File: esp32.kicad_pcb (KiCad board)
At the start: 2 copper layers, 44 x 80 mm, 102 parts, among them J1 USB_C, J14 PWR_CONN, J15 SPI_0, J16 SPI_1, J3 A0, J4 A1, J5 A2, J6 D0, J7 D1, J8 USB_VOUT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

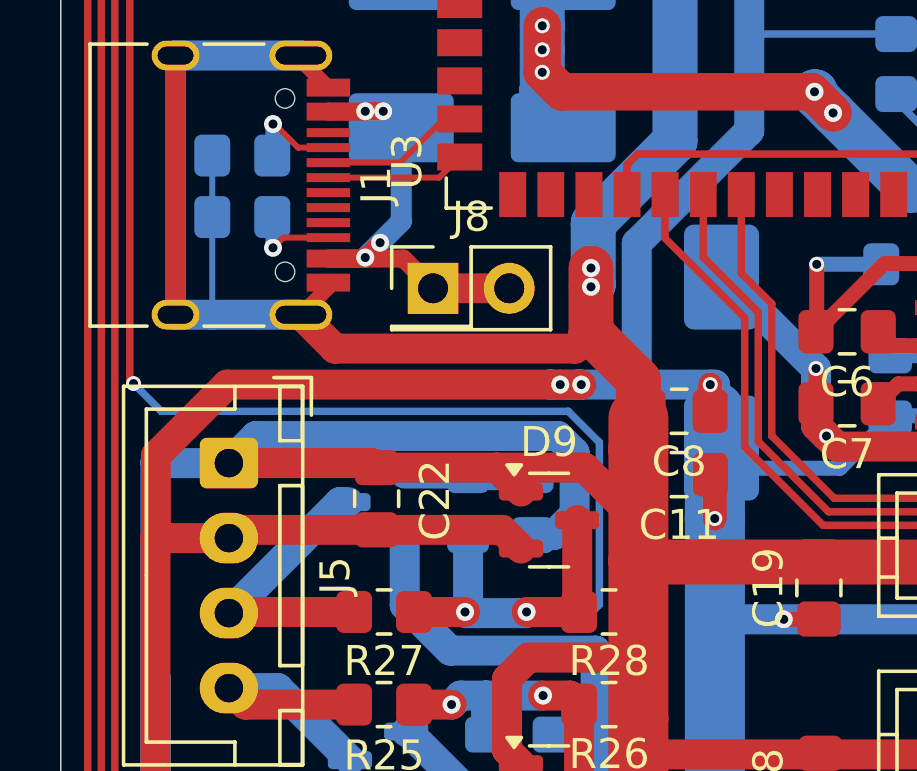
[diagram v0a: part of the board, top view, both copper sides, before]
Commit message: change footprint of Vusb
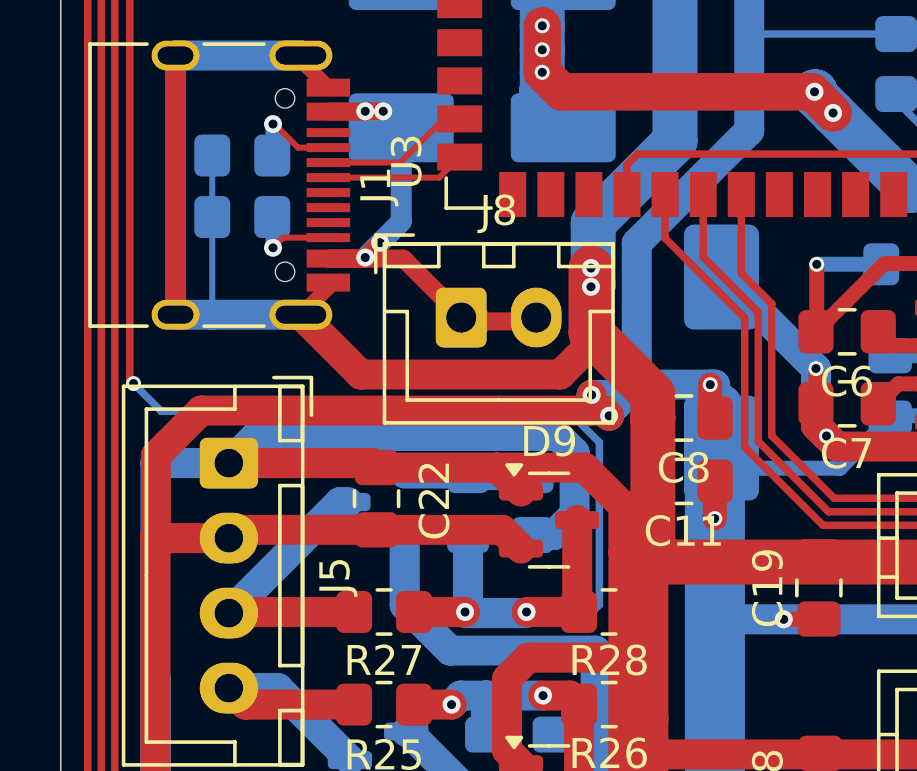
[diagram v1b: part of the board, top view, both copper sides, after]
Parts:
- J8: footprint Connector_PinHeader_2.54mm:PinHeader_2x01_P2.54mm_Vertical -> Connector_JST:JST_XH_B2B-XH-A_1x02_P2.50mm_Vertical
- moved J8 1.35 mm to (84.2, 96.6)
- moved C8 0.28 mm to (91.7, 100.0)
- moved C11 0.28 mm to (91.7, 102.1)
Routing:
- net GND: track 714.9 -> 717.8 mm
- net +3V3: track 446.4 -> 448.5 mm
- net V_USB: track 17.9 -> 19.6 mm

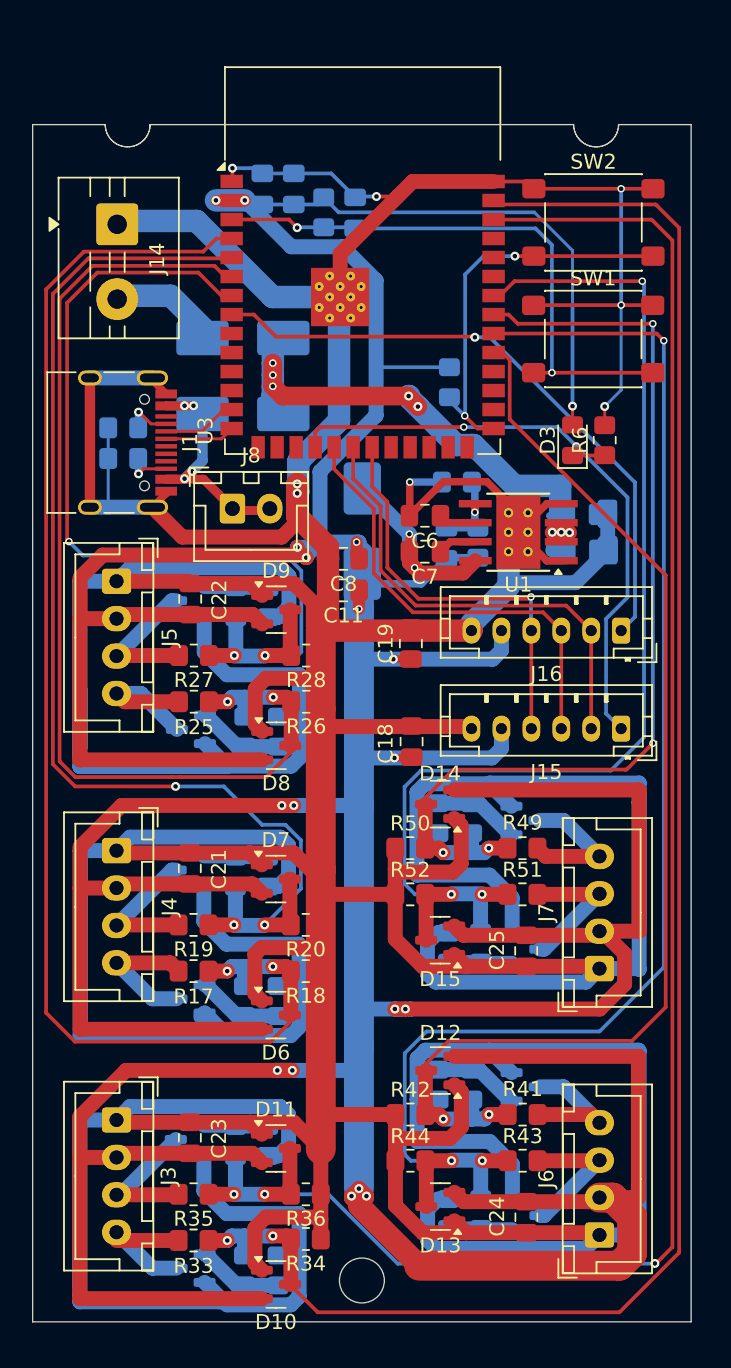
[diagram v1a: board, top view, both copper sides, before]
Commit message: move inductor
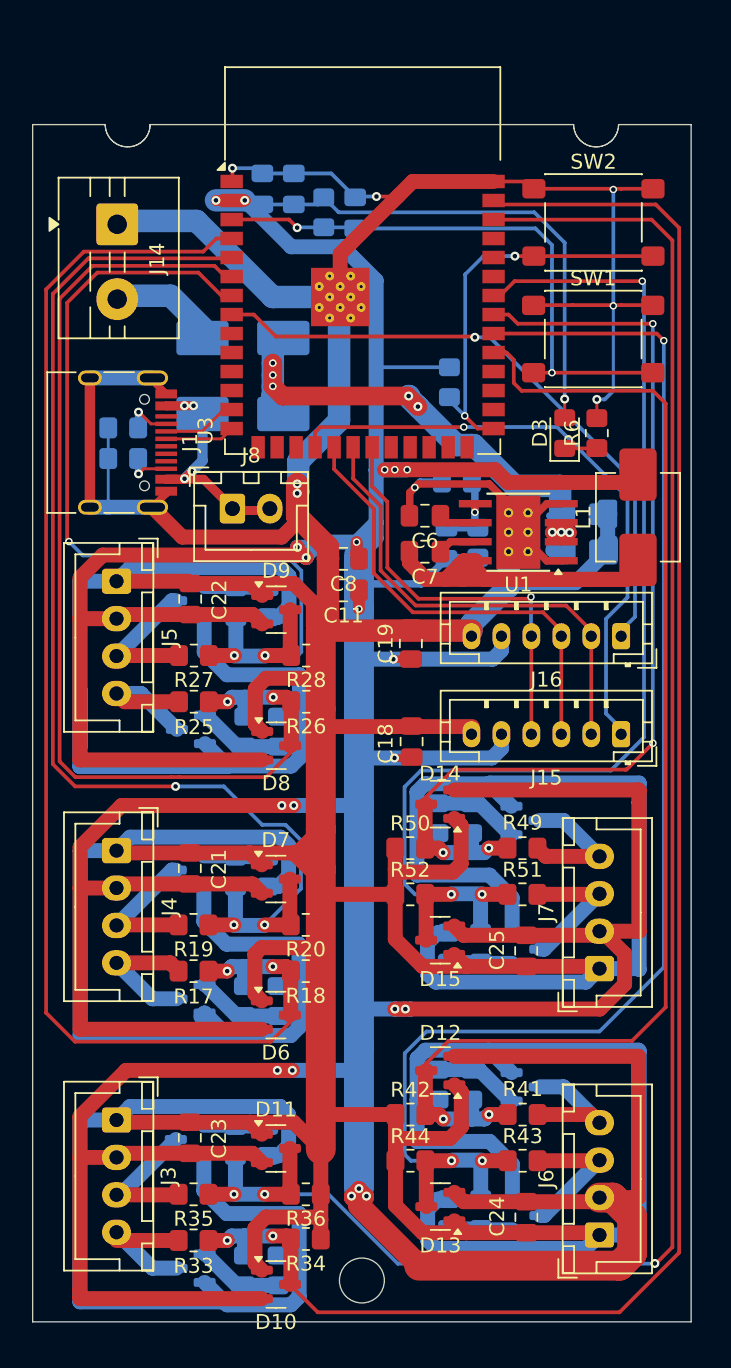
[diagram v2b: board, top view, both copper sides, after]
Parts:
- L1: moved to F.Cu
- moved L1 18.4 mm to (111.3, 97.2), turned to 90 degrees
- moved D3 0.71 mm to (106.4, 91.6)
- moved R6 0.71 mm to (108.6, 91.6)
- moved J15 0.38 mm to (110.2, 111.7)
- moved J16 0.38 mm to (110.2, 105.2)
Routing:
- net +3V3: track 448.5 -> 470.4 mm, vias 18 -> 21
- net Net-(U1-SW): track 13.7 -> 32.9 mm, vias 2 -> 0
- net /D0: track 76.3 -> 82.2 mm
- net GND: track 717.8 -> 718.5 mm

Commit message: fix power supply module layout
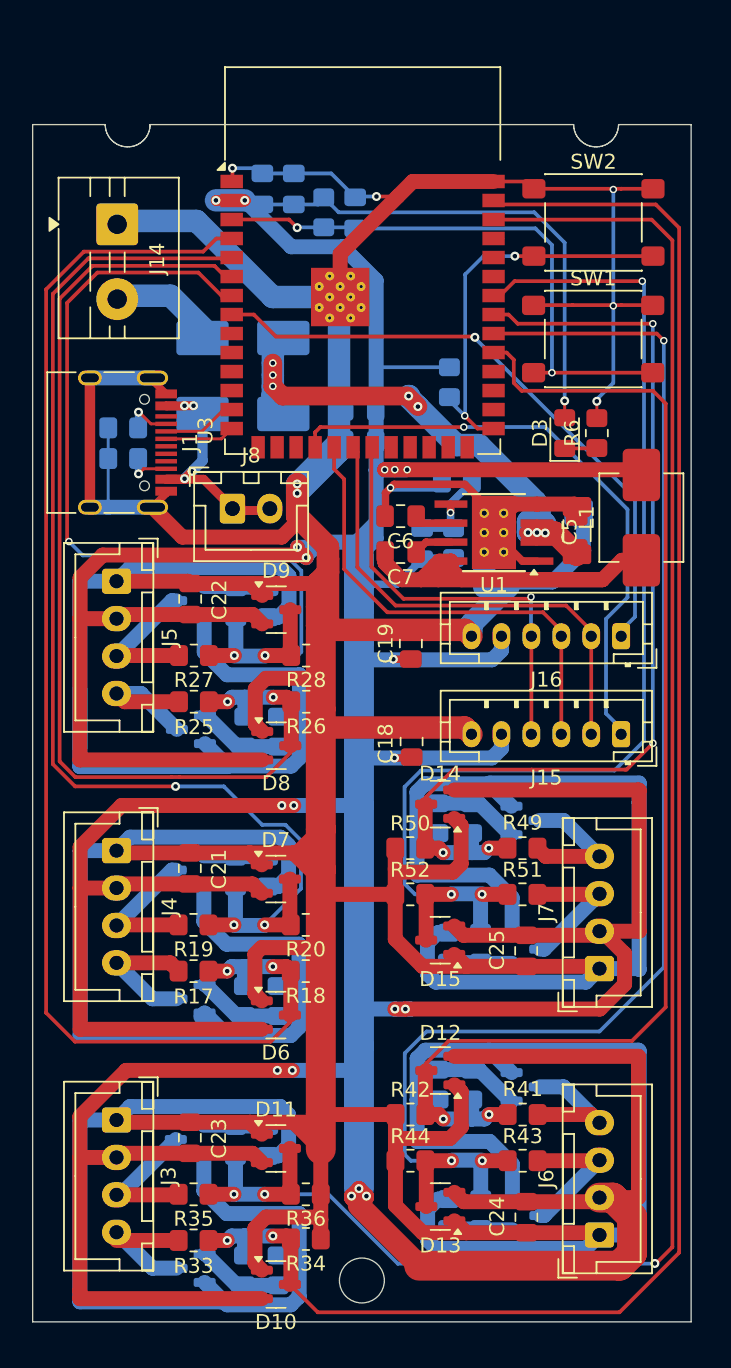
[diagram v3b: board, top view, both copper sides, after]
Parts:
- C11, C8: moved to B.Cu
- C5: moved to F.Cu
- moved C11 12.1 mm to (92.8, 90.0)
- moved C8 7.92 mm to (92.8, 92.1)
- moved C12 1.63 mm to (96.9, 99.0)
- moved C4 1.63 mm to (106.0, 97.0)
- moved C6 1.63 mm to (95.5, 97.1)
- moved C7 1.63 mm to (95.5, 99.5)
- moved R7 1.63 mm to (99.0, 98.9)
- moved U1 1.63 mm to (101.7, 98.2)
- moved C5 1.29 mm to (107.2, 98.2), turned to 90 degrees
- moved L1 0.23 mm to (111.5, 97.2)
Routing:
- net GND: track 718.5 -> 733.7 mm
- net +3V3: track 470.4 -> 468.3 mm, vias 21 -> 19
- net Net-(U1-SW): track 32.9 -> 34.9 mm
- net /SPI_MOSI: track 30.2 -> 31.2 mm
- net /SPI_SCK: track 31.6 -> 32.3 mm
- net Net-(U1-FB): track 5.60 -> 6.35 mm
- net /SPI_CS1: track 42.0 -> 41.4 mm
- net /SPI_MISO: track 27.8 -> 28.4 mm

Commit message: add ground plane
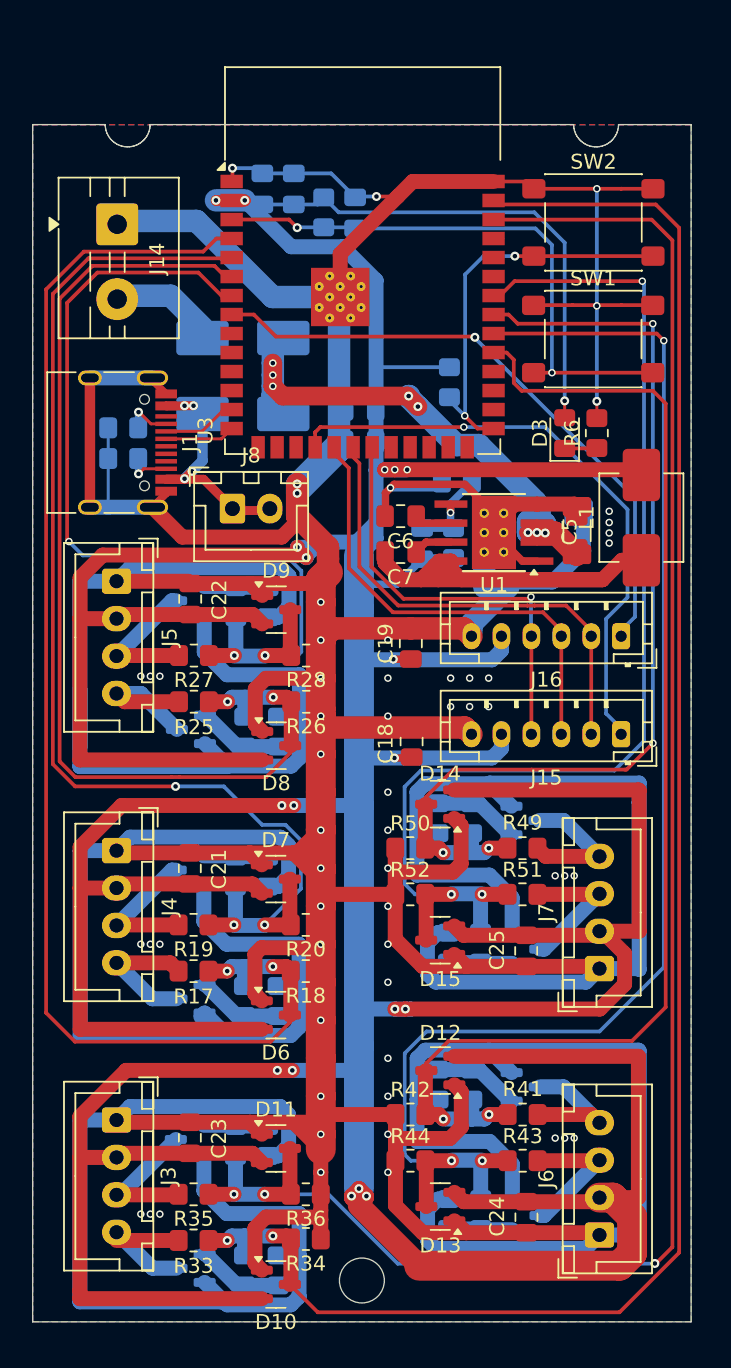
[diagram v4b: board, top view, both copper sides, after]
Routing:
- net GND: track 733.7 -> 728.0 mm, vias 8 -> 59
- added copper zone on B.Cu, net GND
- added copper zone on F.Cu, net GND

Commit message: review passed
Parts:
- removed C12: 20pF, Capacitor_SMD:C_0805_2012Metric_Pad1.18x1.45mm_HandSolder
- removed J14: PWR_CONN, TerminalBlock:TerminalBlock_MaiXu_MX126-5.0-02P_1x02_P5.00mm
- removed SW1: SW_RST, Button_Switch_SMD:SW_SPST_PTS645Sx43SMTR92
- removed SW2: SW_BOOT, Button_Switch_SMD:SW_SPST_PTS645Sx43SMTR92
- added BOOT: SW_BOOT, Button_Switch_SMD:SW_SPST_PTS645Sx43SMTR92, F.Cu at (109.6, 97.5)
- added EN: SW_RST, Button_Switch_SMD:SW_SPST_PTS645Sx43SMTR92, F.Cu at (109.6, 89.8)
- added PWR: PWR_CONN, TerminalBlock:TerminalBlock_MaiXu_MX126-5.0-02P_1x02_P5.00mm, F.Cu at (109.7, 82.2)
- C18, C19, C21, C22, C23, C24, C25: value 100n -> 100nF
- C4: value 4.7uF -> 2.2uF
- C5: footprint Library:C_1206&0805 -> LED_SMD:LED_0805_2012Metric_Pad1.15x1.40mm_HandSolder; moved to B.Cu
- C6, L1, U1: moved to B.Cu
- C7: value 0.1uF -> 100nF; moved to B.Cu
- R1, R2: moved to F.Cu
- moved L1 40.7 mm to (74.2, 81.1)
- moved C5 35.0 mm to (80.4, 75.7), turned to 180 degrees
- moved C4 34.4 mm to (81.9, 72.4), turned to 180 degrees
- moved U1 27.4 mm to (80.5, 80.9), turned to -90 degrees
- moved C8 27.2 mm to (73.8, 72.6), turned to 0 degrees
- moved R7 24.8 mm to (84.7, 78.6), turned to 90 degrees
- moved C11 24.3 mm to (73.8, 74.9), turned to 0 degrees
- moved R2 22.4 mm to (98.6, 97.7), turned to 0 degrees
- moved C7 21.3 mm to (78.8, 86.2)
- moved D1 19.6 mm to (102.8, 77.2), turned to 0 degrees
- moved R53 19.0 mm to (84.7, 82.5), turned to 90 degrees
- moved C6 16.6 mm to (83.0, 86.2), turned to 0 degrees
- moved R1 11.8 mm to (98.6, 99.9), turned to 0 degrees
- moved R6 10.2 mm to (98.5, 93.1), turned to 180 degrees
- moved D3 8.73 mm to (98.6, 95.4), turned to 180 degrees
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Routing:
- net GND: track 728.0 -> 690.4 mm, vias 59 -> 171
- net /EN: track 38.6 -> 64.4 mm, vias 2 -> 4
- net Net-(U1-SW): track 34.9 -> 11.9 mm
- net VCC: track 38.3 -> 48.5 mm, vias 8 -> 0
- net /A5: track 64.3 -> 59.5 mm
- net +3V3: track 468.3 -> 463.9 mm, vias 19 -> 22
- net /SPI_CS0: track 40.0 -> 35.8 mm
- net /D-: track 4.45 -> 8.38 mm
- net /D3: track 79.6 -> 76.4 mm
- net V_USB: track 19.6 -> 22.5 mm, vias 4 -> 2
- net /A2: track 90.3 -> 92.9 mm
- net /D+: track 5.62 -> 8.06 mm
- net Net-(D1-A): track 7.82 -> 5.40 mm
- net /A3: track 81.0 -> 83.4 mm
- net /D1: track 94.5 -> 92.2 mm, vias 3 -> 5
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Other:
- board size 44 x 80 mm -> 44 x 80.5 mm
- board text added: "+"
- board text added: "-"
- board text added: "1"
- board text added: "10"
- board text added: "15"
- board text added: "2"
- board text added: "38"
- board text added: "39"
- board text added: "3V3"
- board text added: "4"
- board text added: "40"
- board text added: "41"
- board text added: "5"
- board text added: "6"
- board text added: "7"
- board text added: "A0"
- board text added: "A1"
- board text added: "A2"
- board text added: "CS"
- board text added: "D0"
- board text added: "D1"
- board text added: "GND"
- board text added: "MISO"
- board text added: "MOSI"
- board text added: "SCK"
- board text added: "SPI0"
- board text added: "SPI1"
- board text added: "V_USB"

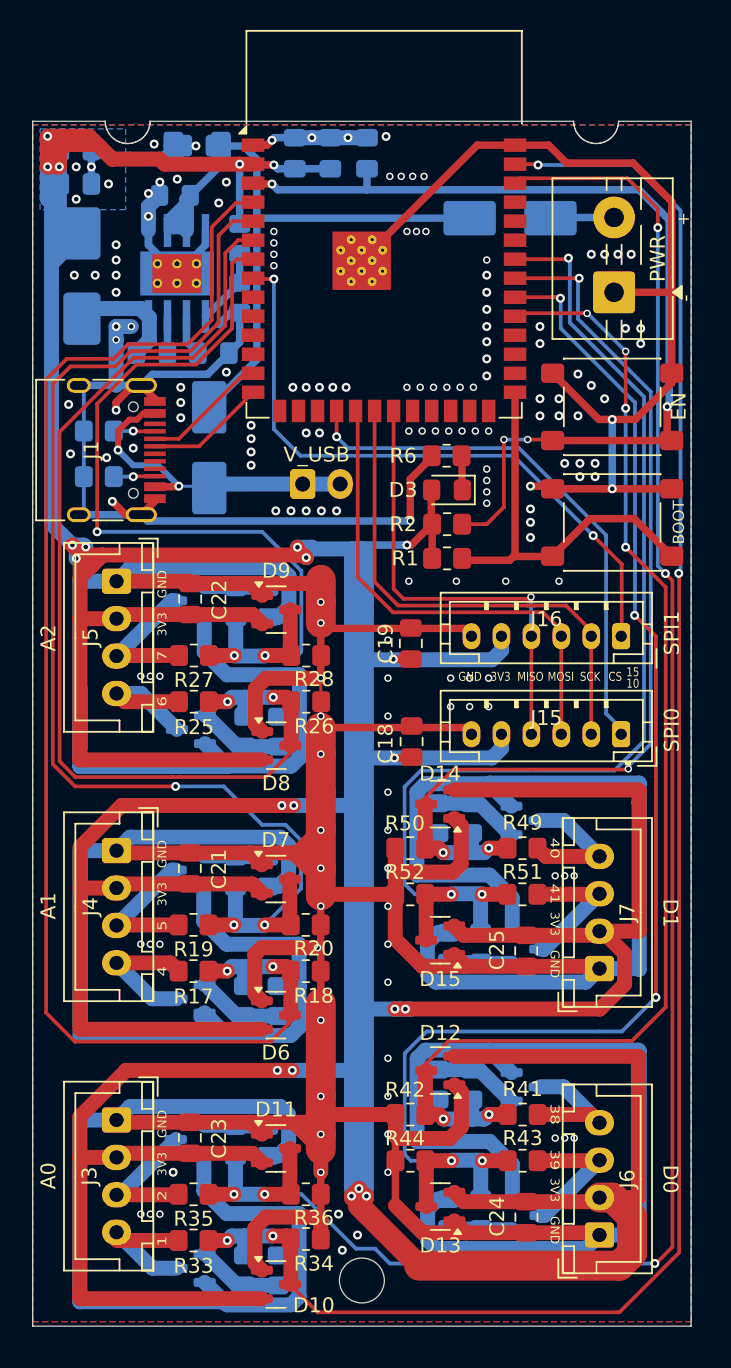
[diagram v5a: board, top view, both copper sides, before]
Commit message: add silkscreen
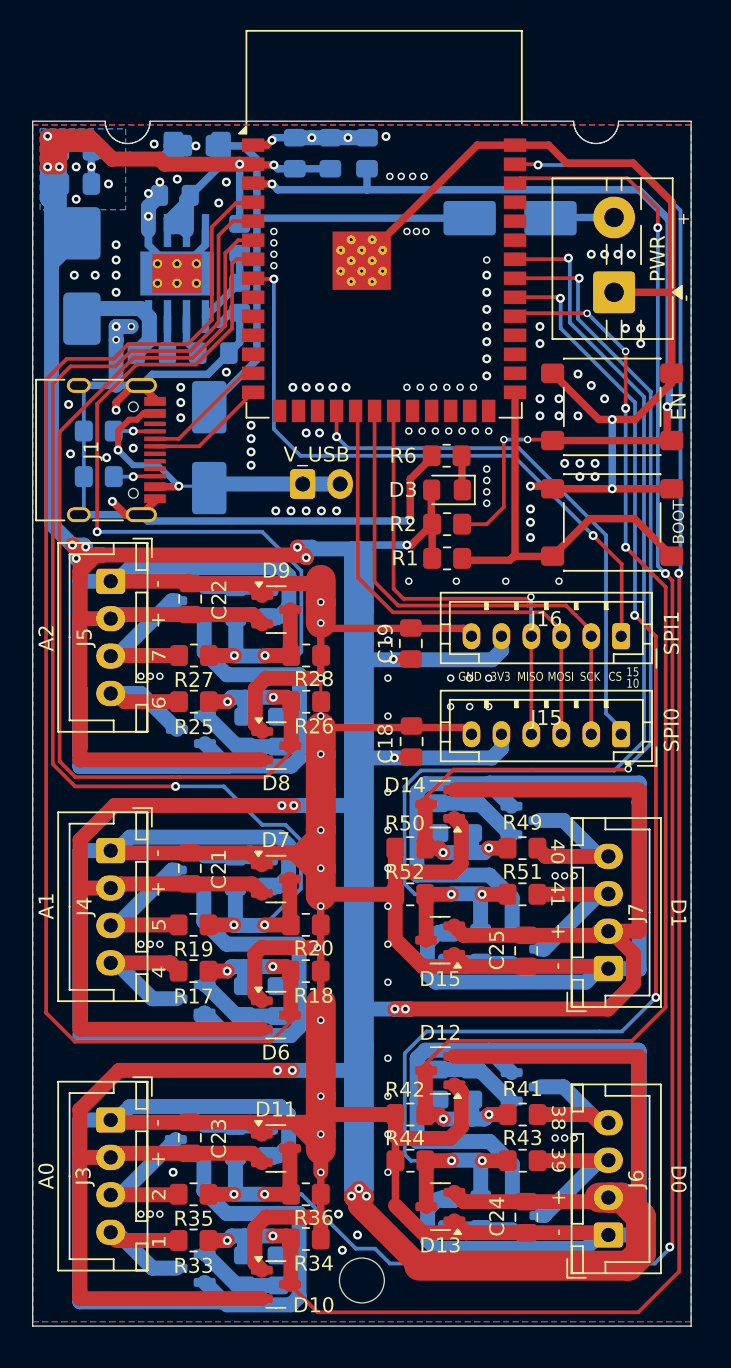
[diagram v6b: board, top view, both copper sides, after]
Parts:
- moved J6 0.59 mm to (109.3, 145.2)
- moved J7 0.59 mm to (109.3, 127.4)
- moved J3 0.39 mm to (76.1, 137.5)
- moved J4 0.39 mm to (76.1, 119.5)
- moved J5 0.39 mm to (76.1, 101.5)
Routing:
- net +3V3: track 463.9 -> 466.9 mm
- net /A0: track 120.5 -> 121.2 mm
